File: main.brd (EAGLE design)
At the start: 50.8 x 50.8 mm, 53 parts, among them U2 SN65HVD32_D_8

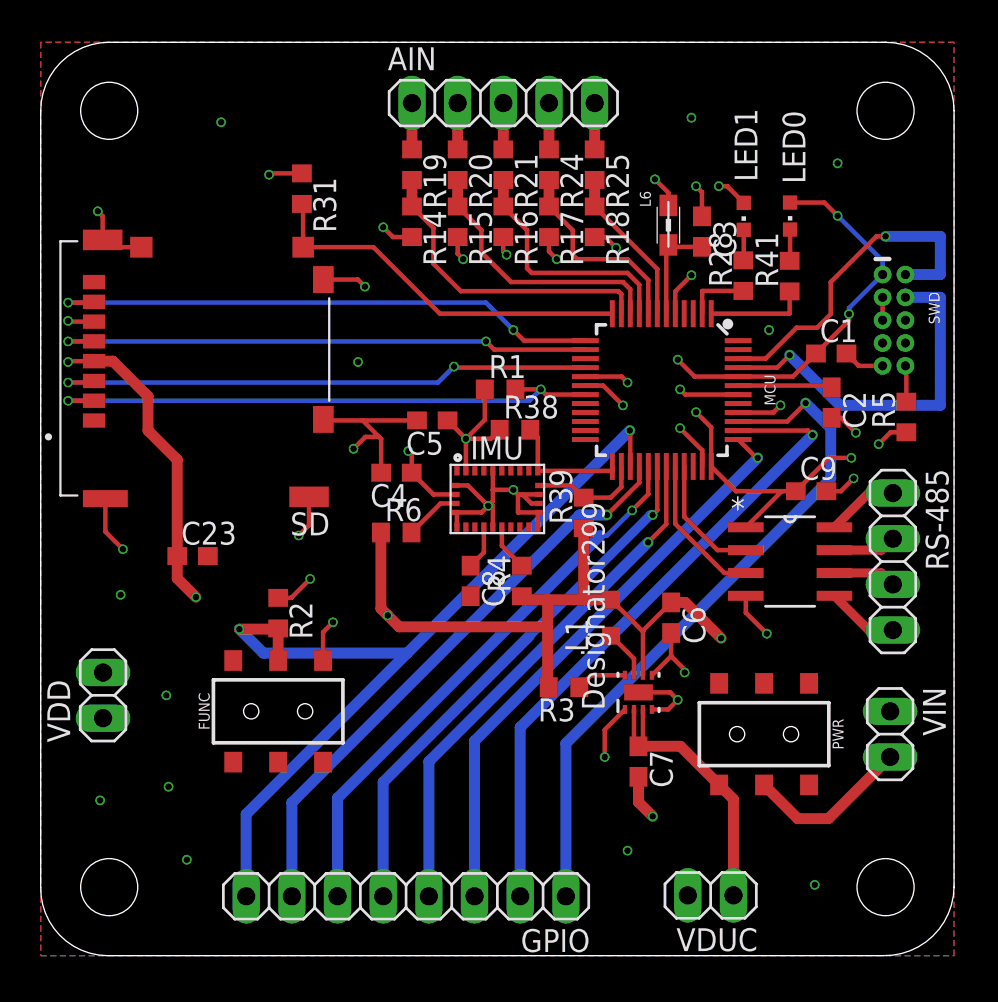
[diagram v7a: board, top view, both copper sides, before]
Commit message: Labeled compenents added logos
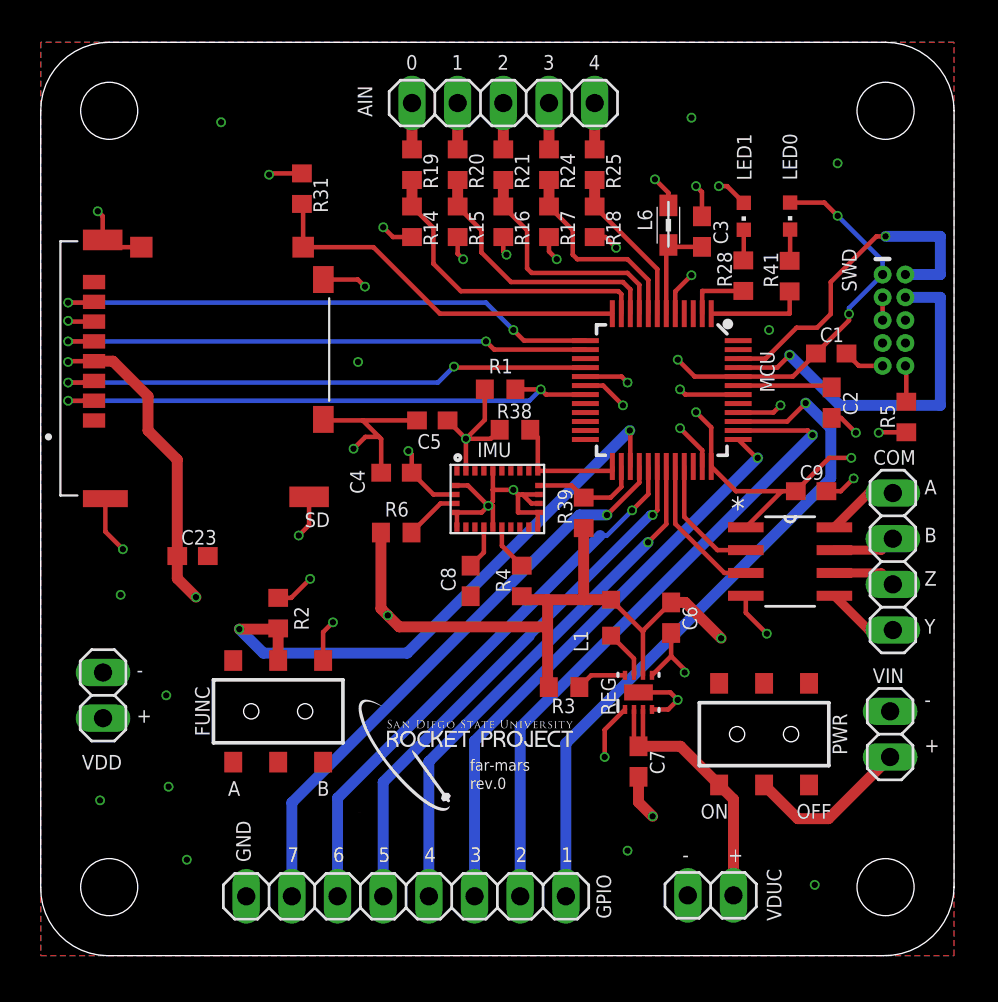
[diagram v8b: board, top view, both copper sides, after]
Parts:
- added U$6: (no value), cool:RP-LOGO-.15
- REG: value (none) -> Value
- renumbered RS-485 to COM, TPS62162-Q1 to REG
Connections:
- net N$11 renamed B
- net N$12 renamed Z
- net N$13 renamed Y
- net N$6 renamed A
- net GND: now also GPIO.8
- net GPIO8: no longer GPIO.8
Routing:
- net GPIO8: track 50.6 -> 33.4 mm
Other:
- board text added: "+"
- board text added: "-"
- board text added: "0"
- board text added: "1"
- board text added: "2"
- board text added: "3"
- board text added: "4"
- board text added: "5"
- board text added: "6"
- board text added: "7"
- board text added: "A"
- board text added: "B"
- board text added: "GND"
- board text added: "OFF"
- board text added: "ON"
- board text added: "Y"
- board text added: "Z"
- board text added: "far-mars"
- board text added: "rev.0"
